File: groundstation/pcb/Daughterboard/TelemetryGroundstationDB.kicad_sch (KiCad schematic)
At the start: 109 parts, among them J1 USB-C, J2 USB-C, J3 ICD15S13E4GV00LF, M1 M4 Mounting Hole, M2 M4 Mounting Hole, M3 M4 Mounting Hole, M4 M4 Mounting Hole, Q1 NPN, U1 CP2102N, U2 CP2102N, U5 AVR128DB64x-xPT

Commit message: add Daugther board schematic
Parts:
- removed C10, C11, C12, C9: 1 uF, Capacitor_SMD:C_0805_2012Metric_Pad1.18x1.45mm_HandSolder, symbol Device:C
- removed C3: 4.7 uF, Capacitor_SMD:C_0805_2012Metric_Pad1.18x1.45mm_HandSolder, symbol Device:C
- removed C4: 0.1 uF, Capacitor_SMD:C_0805_2012Metric_Pad1.18x1.45mm_HandSolder, symbol Device:C
- removed D10: BAT43, Diode_SMD:D_SOD-123, symbol Device:D_Schottky
- removed D18: D, Diode_SMD:D_SOD-123, symbol Device:D
- removed D19, D20, D21, D22, D23, D24, D9: red, LED_SMD:LED_0805_2012Metric_Pad1.15x1.40mm_HandSolder, symbol Device:LED
- removed D25, D26, D27, D28, D3, D7: orange, LED_SMD:LED_0805_2012Metric_Pad1.15x1.40mm_HandSolder, symbol Device:LED
- removed D4: Cree RGB LED, Footprints:Cree RGB LED, symbol Symbols:Cree_RGB_LED
- removed D5, D8: SP0503BAHT, Package_TO_SOT_SMD:SOT-143, symbol Power_Protection:SP0503BAHT
- removed D6: green, LED_SMD:LED_0805_2012Metric_Pad1.15x1.40mm_HandSolder, symbol Device:LED
- removed J1, J2: USB-C, Footprints:GCT_USB4216-03-A_REVA, symbol Symbols:USB4216-03-A_REVA
- removed LS1: Buzzer CMT-0525-75-SMT-TR, Footprints:Buzzer XDCR_CMT-0525-75-SMT-TR, symbol Symbols:Buzzer CMT-0525-75-SMT-TR
- removed Q1: NPN, Package_TO_SOT_SMD:SOT-23, symbol Simulation_SPICE:NPN
- removed R10, R16: 22k, Resistor_SMD:R_0805_2012Metric_Pad1.20x1.40mm_HandSolder, symbol Device:R
- removed R11, R12, R17, R4, R5, R6: 560 Ohm, Resistor_SMD:R_0805_2012Metric_Pad1.20x1.40mm_HandSolder, symbol Device:R
- removed R13, R14, R7, R8: 5k1, Resistor_SMD:R_0805_2012Metric_Pad1.20x1.40mm_HandSolder, symbol Device:R
- removed R15, R9: 47k, Resistor_SMD:R_0805_2012Metric_Pad1.20x1.40mm_HandSolder, symbol Device:R
- removed R18, R19: 470 Ohm, Resistor_SMD:R_0805_2012Metric_Pad1.20x1.40mm_HandSolder, symbol Device:R
- removed R29: 180 R, Resistor_SMD:R_0805_2012Metric_Pad1.20x1.40mm_HandSolder, symbol Device:R
- removed R30, R31, R37, R39, R40, R42, R49, R50: 5k6, Resistor_SMD:R_0805_2012Metric_Pad1.20x1.40mm_HandSolder, symbol Device:R
- removed R32, R33, R35, R36, R43, R44: 1k, Resistor_SMD:R_0805_2012Metric_Pad1.20x1.40mm_HandSolder, symbol Device:R
- removed R45, R46, R47, R48: 270R, Resistor_SMD:R_0805_2012Metric_Pad1.20x1.40mm_HandSolder, symbol Device:R
- removed TP1, TP12, TP13, TP14, TP15, TP16, TP17, TP2, TP3, TP36, TP37, TP38, TP39, TP9: TestPoint, Footprints:Test Point, symbol Connector:TestPoint
- removed U1, U2: CP2102N, Footprints:QFN20_CP2102N_SIL, symbol Interface_USB:CP2102N-Axx-xQFN20
- removed U5: AVR128DB64x-xPT, Package_QFP:TQFP-64_10x10mm_P0.5mm, symbol MCU_Microchip_AVR_Dx:AVR128DB64x-xPT
- added J1: RFPC-SMA27-F, Footprints:GRADCONN_RFPC-SMA27-F, symbol Symbols:RFPC-SMA27-F
- added U1: RC1780HP-RC232, Footprints:Radiocrafts RC1780HP-RC232, symbol Symbols:Radiocrafts RC1780HP-RC232
- added ZP1, ZS1: ~, Resistor_SMD:R_0805_2012Metric_Pad1.20x1.40mm_HandSolder, symbol Device:R
- C1: value 4.7 uF -> 1 nF; Digikey Link (none) -> https://www.digikey.de/de/products/detail/samsung-electro-m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; Purchase-URL (none) -> https://www.digikey.de/de/products/detail/samsung-electro-m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
- C2: value 0.1 uF -> 1 uf
- D1: value orange -> green; Digikey Link (none) -> https://www.digikey.de/de/products/detail/liteon/LTST-C171G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; Purchase-URL (none) -> https://www.digikey.de/de/products/detail/liteon/LTST-C171G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
- D2: value orange -> yellow; Digikey Link (none) -> https://www.digikey.de/de/products/detail/liteon/LTST-C171Y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; Purchase-URL (none) -> https://www.digikey.de/de/products/detail/liteon/LTST-C171Y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
- D3: renamed from D11; now fitted
- D4: renamed from D12; now fitted
- R1: value 560 Ohm -> 2k7; Digikey Link (none) -> https://www.digikey.de/de/products/detail/yageo/RC0805JR-07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; Purchase-URL (none) -> https://www.digikey.de/de/products/detail/yageo/RC0805JR-07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
- R2, R3: value 560 Ohm -> 560R; Digikey Link (none) -> https://www.digikey.de/de/products/detail/yageo/RC0805JR-07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; Purchase-URL (none) -> https://www.digikey.de/de/products/detail/yageo/RC0805JR-07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
- R7: renamed from R20; now fitted
- R8: renamed from R21; now fitted
- renumbered D13 to D5, J3 to J2, R41 to R4, R38 to R5, R34 to R6, TP70 to TP1, TP80 to TP2, TP60 to TP3, TP8 to TP6
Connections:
- net D2 is gone; now on net CTS: J2.2
- net D3 is gone; now on net CFG: J2.3
- net LED 2 is gone; now on an unnamed net: R2.1
- net RST1 is gone; now on net RST: R5.1, TP3.1
- net RTS1 is gone; now on net RTS: TP6.1
- net RX0 is gone; now on net RX: TP2.1
- net TX0 is gone; now on net TX: R6.1, TP1.1
- net +3V3: now also JP2.1 (A), U1.13 (VCC); no longer C1.1
- net +5V: now also JP1.1 (A)
- net GND: now also J1.G1, J1.G2, J1.G3, J1.G4, U1.1 (GND), U1.10 (GND), U1.14 (GND), U1.7 (GND), U1.8 (GND), ZP1.2; no longer JP1.2 (B), JP2.2 (B)
- net RX: now also U1.5 (TXD)
- net TX: now also U1.6 (RXD)
- net at R3.2: now also U1.30 (D2)
- net at R2.2: now also U1.29 (D1); no longer D2.2 (A)
- net at D1.2 (A): no longer R1.2
- net CFG1 renamed CFG
- net CFG: now also U1.4 (CONFIG)
- net CTS1 renamed CTS
- net CTS: now also U1.2 (CTS/RXTX)
- net D1 renamed RTS
- net RTS: now also U1.3 (RTS/SLEEP)
- net D4 renamed RST
- net RST: now also R1.2
- net LED 1: no longer names the net of R1.1
- net LED 1: now also C1.1, U1.12 (RESET)
- net LED 3: no longer names the net of R3.1
- net LED 3: now also D2.2 (A)
- new net: JP1.2 (B), JP2.2 (B), U1.41 (VCC_PA)
- new net: U1.9 (RF), ZS1.1
- new net: J1.1, ZP1.1, ZS1.2
- no-connect marks 36 -> 2
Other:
- note added: "ESD Protection"
- note added: "HD15 D-Sub Connector"
- note added: "Radio module"
- note removed: "Buzzer"
- note removed: "Microcontroller"
- note removed: "Pinheader?"
- note removed: "Status LEDs"
- note removed: "USB UART"
- note removed: "USB UPDI"
- moved on the sheet: D5, J2, M1, M2, M3, M4, R4, R5, R6, TP1, TP2, TP3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

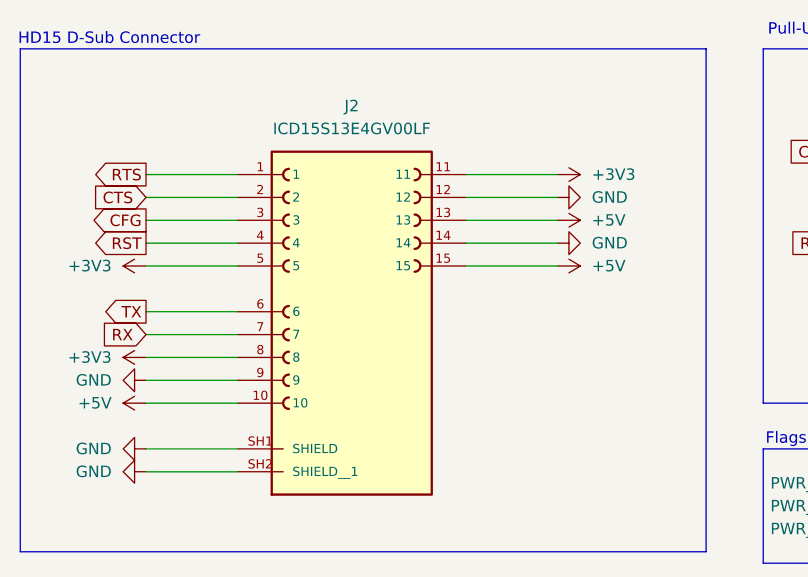
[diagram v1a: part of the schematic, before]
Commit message: change hd15 pin positions
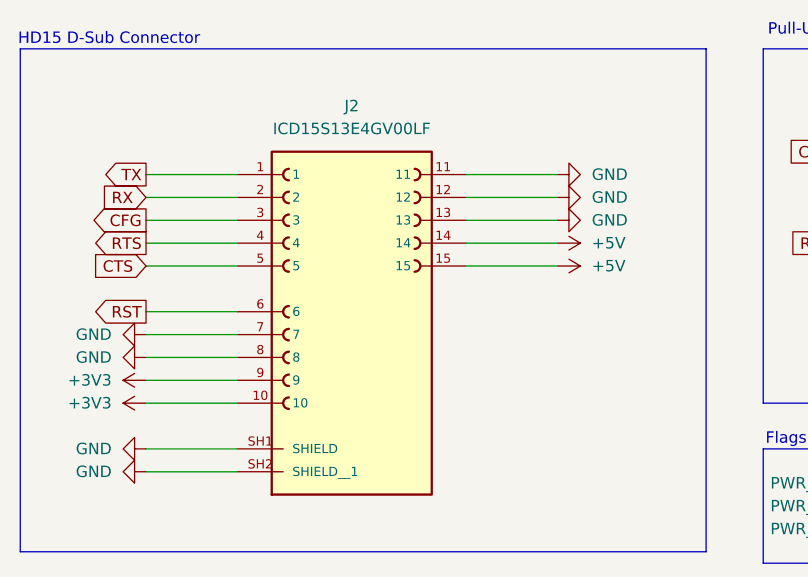
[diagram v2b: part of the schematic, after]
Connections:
- net +3V3: now also J2.10, J2.9; no longer J2.11, J2.5, J2.8
- net +5V: now also J2.14; no longer J2.10, J2.13
- net CTS: now also J2.5; no longer J2.2
- net GND: now also J2.11, J2.13, J2.7, J2.8; no longer J2.14, J2.9
- net RST: now also J2.6; no longer J2.4
- net RTS: now also J2.4; no longer J2.1
- net RX: now also J2.2; no longer J2.7
- net TX: now also J2.1; no longer J2.6

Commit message: add drawing sheet informations
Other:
- company: (none) -> Spaceflight Rocketry Giessen e.V.
- title: (none) -> Telemetry Groundstation Daughterboard PCB
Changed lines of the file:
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@@
 	(generator_version "9.0")
 	(paper "A4" portrait)
+	(title_block
+		(title "Telemetry Groundstation Daughterboard PCB")
+		(date "2026-03-01")
+		(company "Spaceflight Rocketry Giessen e.V.")
+	)
 	(rectangle
 		(start 146.05 144.78)

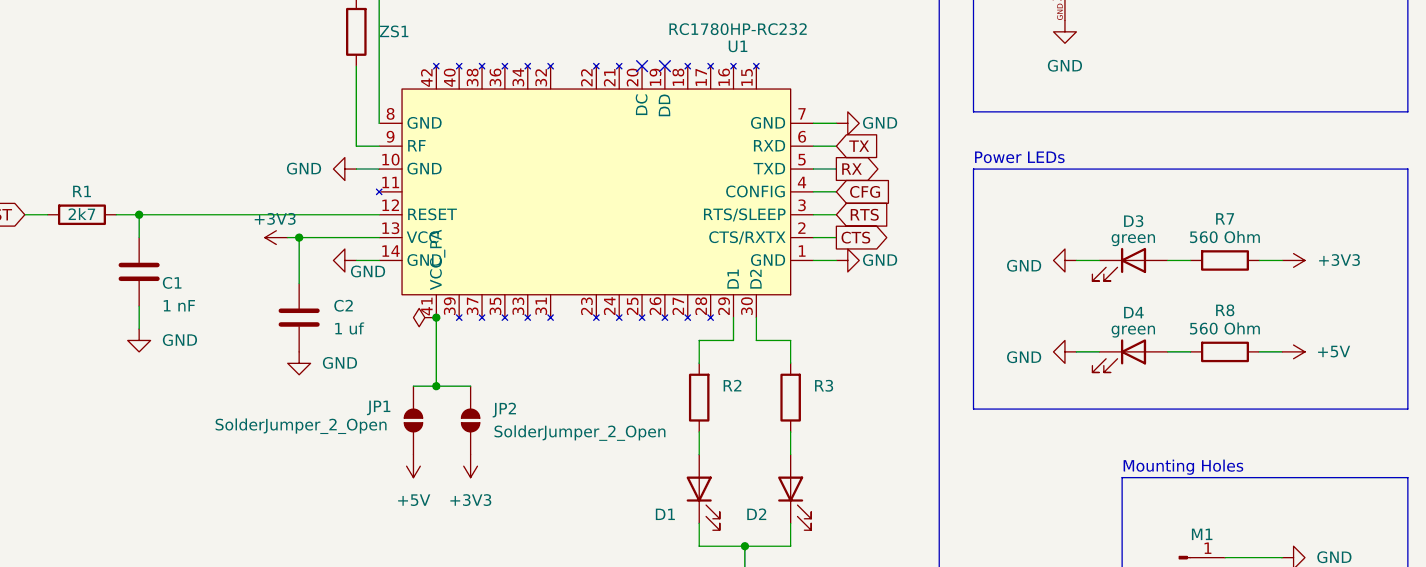
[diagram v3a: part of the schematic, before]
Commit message: add Digikey purchase links for Daughter- and Motherboard
fixes #30
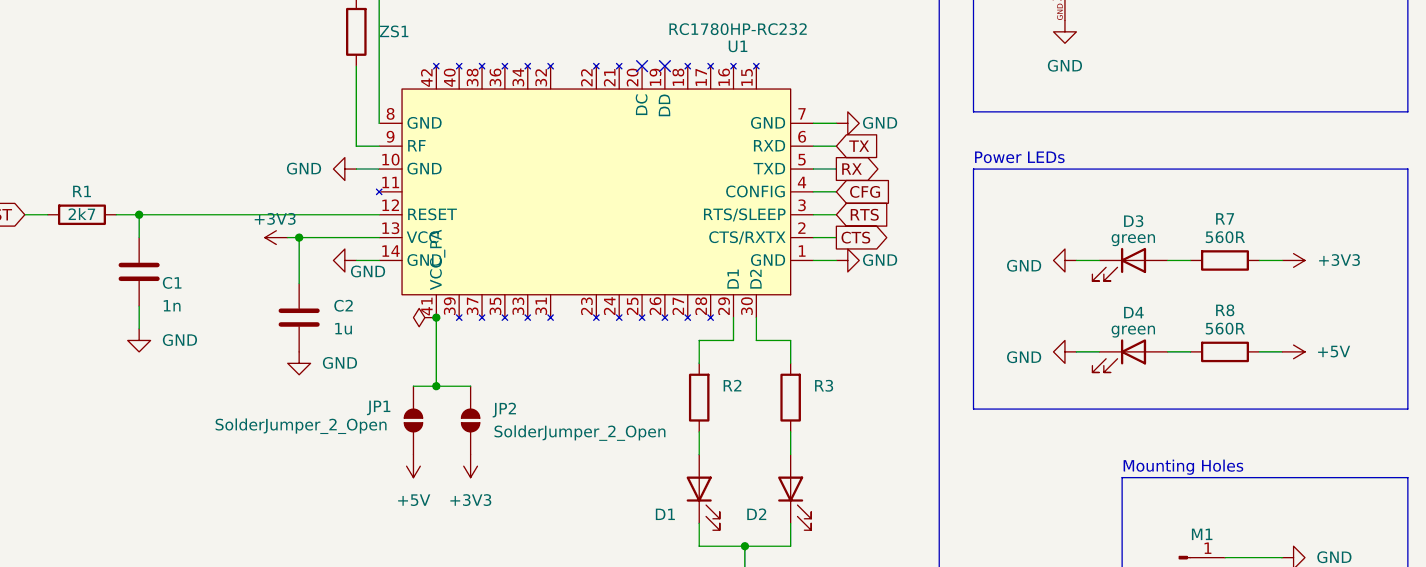
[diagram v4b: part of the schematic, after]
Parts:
- C1: value 1 nF -> 1n; Purchase-URL https://www.digikey.de/de/products/detail/samsung-electro-mechanics/CL21B102KBANNNC/3886678 -> https://www.digikey.de/de/products/detail/samsung-electro-mechanics/CL21B102KCANNNC/3886827
- C2: value 1 uf -> 1u; Purchase-URL (none) -> https://www.digikey.de/de/products/detail/samsung-electro-m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
- D1: Purchase-URL https://www.digikey.de/de/products/detail/liteon/LTST-C171G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 -> https://www.digikey.de/de/products/detail/liteon/LTST-C171K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
- D2: Purchase-URL https://www.digikey.de/de/products/detail/liteon/LTST-C171Y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 -> https://www.digikey.de/de/products/detail/liteon/LTST-C170K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
- D3, D4: Purchase-URL (none) -> https://www.digikey.de/de/products/detail/liteon/LTST-C171K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
- D5: Purchase-URL (none) -> https://www.digikey.de/de/products/detail/w%C3%BCrth-elektr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
- J1: Purchase-URL (none) -> https://www.digikey.de/de/products/detail/gct/RFPC-SMA27-F/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
- J2: Purchase-URL (none) -> https://www.digikey.de/de/products/detail/amphenol-cs-fci/I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
- R1, R2, R3: Purchase-URL https://www.digikey.de/de/products/detail/yageo/RC0805JR-07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 -> https://www.digikey.de/de/products/detail/stackpole-electro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
- R4, R5, R6: Purchase-URL (none) -> https://www.digikey.de/de/products/detail/stackpole-electro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
- R7, R8: value 560 Ohm -> 560R; Purchase-URL (none) -> https://www.digikey.de/de/products/detail/stackpole-electro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
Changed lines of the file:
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@@
 			)
 		)
+		(property "Purchase-URL" "~"
+			(at 152.4 104.14 0)
+			(effects
+				(font
+					(size 1.27 1.27)
+				)
+				(hide yes)
+			)
+		)
 		(pin "1"
 		)
@@
 			)
 		)
+		(property "Purchase-URL" "https://www.digikey.de/de/products/detail/liteon/LTST-C171KGKT/386799"
+			(at 147.32 71.12 0)
+			(effects
+				(font
+					(size 1.27 1.27)
+				)
+				(hide yes)
+			)
+		)
 		(pin "1"
 		)
@@
 			)
 		)
+		(property "Purchase-URL" "https://www.digikey.de/de/products/detail/stackpole-electronics-inc/RMCF0805JT5K60/1757920"
+			(at 113.03 134.62 90)
+			(effects
+				(font
+					(size 1.27 1.27)
+				)
+				(hide yes)
+			)
+		)
 		(pin "1"
 		)
@@
 			)
 		)
-		(property "Purchase-URL" "https://www.digikey.de/de/products/detail/liteon/LTST-C171GKT/386793"
+		(property "Purchase-URL" "https://www.digikey.de/de/products/detail/liteon/LTST-C171KGKT/386799"
 			(at 99.06 96.52 90)
 			(effects
@@
 			)
 		)
+		(property "Purchase-URL" "~"
+			(at 156.21 165.1 90)
+			(effects
+				(font
+					(size 1.27 1.27)
+				)
+				(hide yes)
+			)
+		)
 		(pin "1"
 		)
@@
 			)
 		)
+		(property "Purchase-URL" "https://www.digikey.de/de/products/detail/stackpole-electronics-inc/RMCF0805JT5K60/1757920"
+			(at 113.03 144.78 90)
+			(effects
+				(font
+					(size 1.27 1.27)
+				)
+				(hide yes)
+			)
+		)
 		(pin "1"
 		)
@@
 			)
 		)
+		(property "Purchase-URL" "https://www.digikey.de/de/products/detail/stackpole-electronics-inc/RMCF0805JT5K60/1757920"
+			(at 114.3 154.94 90)
+			(effects
+				(font
+					(size 1.27 1.27)
+				)
+				(hide yes)
+			)
+		)
 		(pin "1"
 		)
@@
 			)
 		)
-		(property "Purchase-URL" "https://www.digikey.de/de/products/detail/liteon/LTST-C171YKT/386807"
+		(property "Purchase-URL" "https://www.digikey.de/de/products/detail/liteon/LTST-C170KSKT/386781"
 			(at 109.22 96.52 90)
 			(effects
@@
 			)
 		)
-		(property "Value" "560 Ohm"
+		(property "Value" "560R"
 			(at 157.48 68.58 90)
 			(effects
@@
 			)
 		)
+		(property "Purchase-URL" "https://www.digikey.de/de/products/detail/stackpole-electronics-inc/RMCF0805JT560R/1757876"
+			(at 157.48 71.12 90)
+			(effects
+				(font
+					(size 1.27 1.27)
+				)
+				(hide yes)
+			)
+		)
 		(pin "1"
 		)
@@
 			)
 		)
+		(property "Purchase-URL" "~"
+			(at 154.94 170.18 90)
+			(effects
+				(font
+					(size 1.27 1.27)
+				)
+				(hide yes)
+			)
+		)
 		(pin "1"
 		)
@@
 			)
 		)
+		(property "Purchase-URL" "~"
+			(at 152.4 127 0)
+			(effects
+				(font
+					(size 1.27 1.27)
+				)
+				(hide yes)
+			)
+		)
 		(pin "1"
 		)
@@
 			)
 		)
+		(property "Purchase-URL" "https://www.digikey.de/de/products/detail/liteon/LTST-C171KGKT/386799"
+			(at 147.32 81.28 0)
+			(effects
+				(font
+					(size 1.27 1.27)
+				)
+				(hide yes)
+			)
+		)
 		(pin "1"
 		)
@@
 			)
 		)
-		(property "Value" "1 nF"
+		(property "Value" "1n"
 			(at 39.37 76.2 0)
 			(effects
@@
 			)
 		)
-		(property "Purchase-URL" "https://www.digikey.de/de/products/detail/samsung-electro-mechanics/CL21B102KBANNNC/3886678"
+		(property "Purchase-URL" "https://www.digikey.de/de/products/detail/samsung-electro-mechanics/CL21B102KCANNNC/3886827"
 			(at 36.83 72.39 0)
 			(effects
@@
 			)
 		)
-		(property "Purchase-URL" "https://www.digikey.de/de/products/detail/yageo/RC0805JR-07270RL/728291"
+		(property "Purchase-URL" "https://www.digikey.de/de/products/detail/stackpole-electronics-inc/RMCF0805JT560R/1757876"
 			(at 109.22 86.36 0)
 			(effects
@@
 			)
 		)
-		(property "Purchase-URL" "https://www.digikey.de/de/products/detail/yageo/RC0805JR-07270RL/728291"
+		(property "Purchase-URL" "https://www.digikey.de/de/products/detail/stackpole-electronics-inc/RMCF0805JT560R/1757876"
 			(at 99.06 86.36 0)
 			(effects
@@
 			)
 		)
+		(property "Purchase-URL" "~"
+			(at 152.4 119.38 0)
+			(effects
+				(font
+					(size 1.27 1.27)
+				)
+				(hide yes)
+			)
+		)
 		(pin "1"
 		)
@@
 			)
 		)
+		(property "Purchase-URL" "~"
+			(at 156.21 160.02 90)
+			(effects
+				(font
+					(size 1.27 1.27)
+				)
+				(hide yes)
+			)
+		)
 		(pin "1"
 		)
@@
 			)
 		)
+		(property "Purchase-URL" "~"
+			(at 154.94 175.26 90)
+			(effects
+				(font
+					(size 1.27 1.27)
+				)
+				(hide yes)
+			)
+		)
 		(pin "1"
 		)
@@
 			)
 		)
+		(property "Purchase-URL" "https://www.digikey.de/de/products/detail/amphenol-cs-fci/ICD15S13E4GV00LF/1536418?s=N4IgTCBcDaIJIGEAiBGArAZRQZgKIBYBxANQAZSAZAMRAF0BfIA"
+			(at 52.07 152.4 0)
+			(effects
+				(font
+					(size 1.27 1.27)
+				)
+				(hide yes)
+			)
+		)
 		(pin "9"
 		)
@@
 			)
 		)
-		(property "Value" "560 Ohm"
+		(property "Value" "560R"
 			(at 157.48 78.74 90)
 			(effects
@@
 			)
 		)
+		(property "Purchase-URL" "https://www.digikey.de/de/products/detail/stackpole-electronics-inc/RMCF0805JT560R/1757876"
+			(at 157.48 81.28 90)
+			(effects
+				(font
+					(size 1.27 1.27)
+				)
+				(hide yes)
+			)
+		)
 		(pin "1"
 		)
@@
 			)
 		)
+		(property "Purchase-URL" "~"
+			(at 156.21 154.94 90)
+			(effects
+				(font
+					(size 1.27 1.27)
+				)
+				(hide yes)
+			)
+		)
 		(pin "1"
 		)
@@
 			)
 		)
-		(property "Value" "1 uf"
+		(property "Value" "1u"
 			(at 58.42 78.7399 0)
 			(effects
@@
 			)
 		)
+		(property "Purchase-URL" "https://www.digikey.de/de/products/detail/samsung-electro-mechanics/CL21B102KCANNNC/3886827"
+			(at 54.61 77.47 0)
+			(effects
+				(font
+					(size 1.27 1.27)
+				)
+				(hide yes)
+			)
+		)
 		(pin "1"
 		)
@@
 			)
 		)
+		(property "Purchase-URL" "~"
+			(at 156.21 149.86 90)
+			(effects
+				(font
+					(size 1.27 1.27)
+				)
+				(hide yes)
+			)
+		)
 		(pin "1"
 		)
@@
 			)
 		)
+		(property "Purchase-URL" "~"
+			(at 152.4 111.76 0)
+			(effects
+				(font
+					(size 1.27 1.27)
+				)
+				(hide yes)
+			)
+		)
 		(pin "1"
 		)
@@
 			)
 		)
+		(property "Purchase-URL" "https://www.digikey.de/de/products/detail/w%C3%BCrth-elektronik/824021/3900544"
+			(at 139.7 36.83 90)
+			(effects
+				(font
+					(size 1.27 1.27)
+				)
+				(hide yes)
+			)
+		)
 		(pin "1"
 		)
@@
 			)
 		)
-		(property "Purchase-URL" "https://www.digikey.de/de/products/detail/yageo/RC0805JR-072K7L/728277"
+		(property "Purchase-URL" "https://www.digikey.de/de/products/detail/stackpole-electronics-inc/RMCF0805JT2K70/1757901"
 			(at 30.48 66.04 90)
 			(effects
@@
 				(hide yes)
 			)
+		)
+		(property "Purchase-URL" "https://www.digikey.de/de/products/detail/gct/RFPC-SMA27-F/22162144"
+			(at 48.26 27.94 0)
+			(effects
+				(font
+					(size 1.27 1.27)
+				)
+				(hide yes)
+			)
